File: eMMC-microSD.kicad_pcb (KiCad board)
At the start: 4 copper layers, 95 x 41.5 mm, 197 parts, among them J1 Micro_SD_Card, J2 Micro_SD_Card, J3 Micro_SD_Card, J4 Micro_SD_Card, J5 Micro_SD_Card, U1 eMMC_5.1_BGA153, U2 eMMC_5.1_BGA153, U3 eMMC_5.1_BGA153, U4 eMMC_5.1_BGA153, U5 eMMC_5.1_BGA153

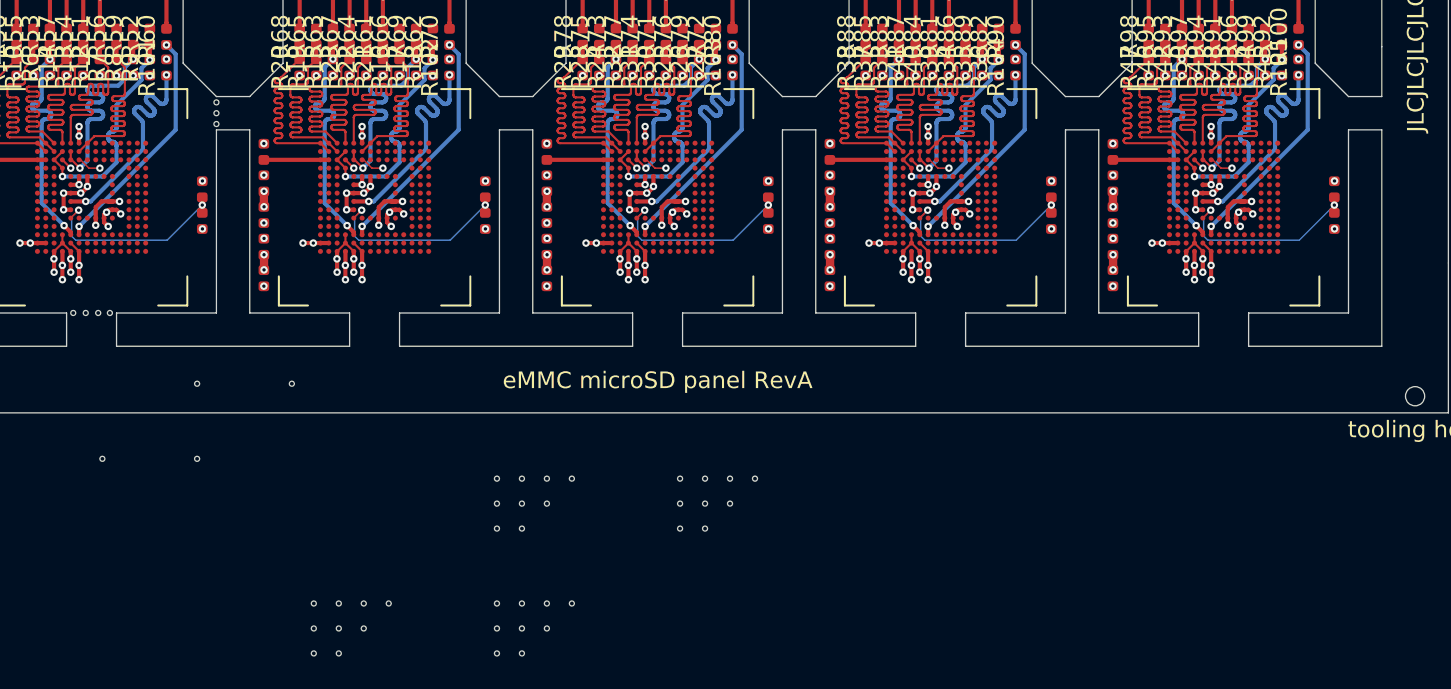
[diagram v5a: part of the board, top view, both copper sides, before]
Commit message: Plce remaining tooling holes
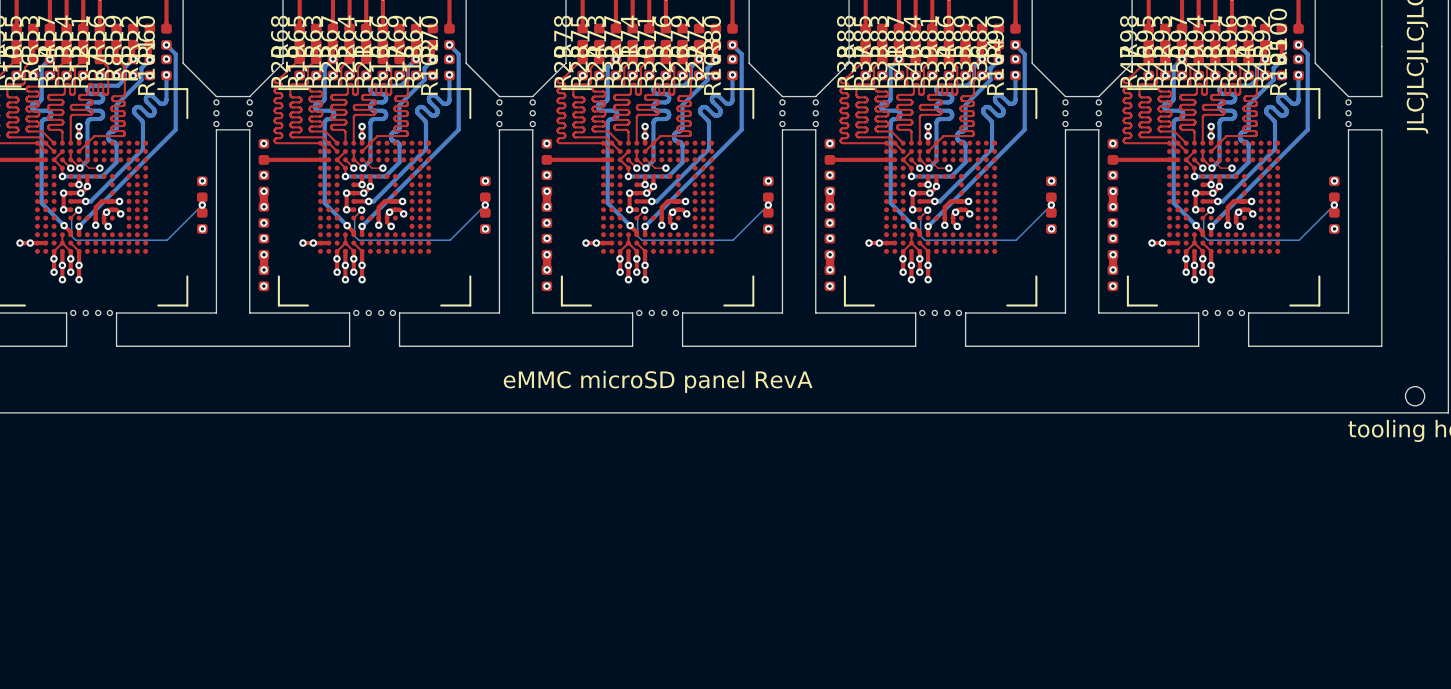
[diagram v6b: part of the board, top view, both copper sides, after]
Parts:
- moved H52 56.5 mm to (162.9, 148.0)
- moved H35 47.1 mm to (153.0, 136.0)
- moved H32 46.5 mm to (153.0, 135.3)
- moved H51 45.9 mm to (145.9, 148.0)
- moved H45 45.7 mm to (170.0, 136.7)
- moved H41 44.8 mm to (170.0, 135.3)
- moved H36 43.5 mm to (153.0, 136.7)
- moved H44 43.2 mm to (170.0, 136.0)
- moved H38 36.4 mm to (138.0, 136.0), turned to 90 degrees
- moved H34 36.2 mm to (138.0, 135.3), turned to 90 degrees
- moved H42 34.8 mm to (162.2, 148.0)
- moved H14 34.5 mm to (119.0, 135.3)
- moved H31 34.3 mm to (138.0, 136.7), turned to 90 degrees
- moved H40 33.9 mm to (155.0, 136.7), turned to 90 degrees
- moved H43 33.8 mm to (155.0, 135.3), turned to 90 degrees
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
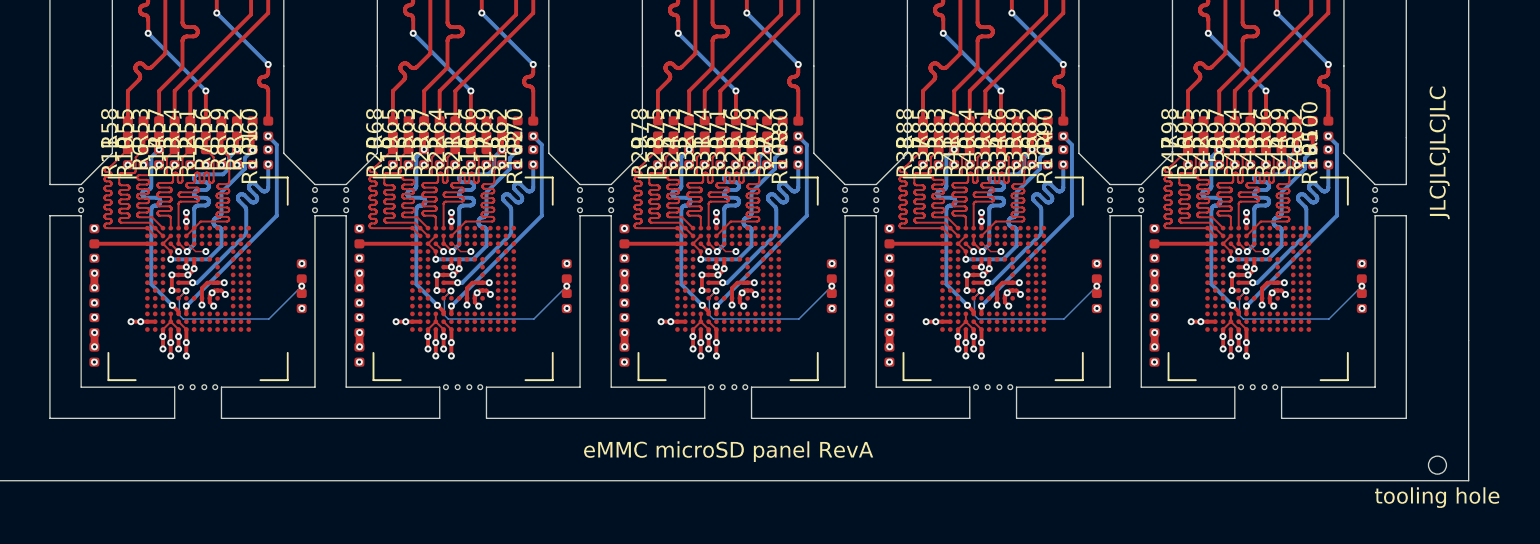
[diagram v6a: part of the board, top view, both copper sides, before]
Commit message: Hide all references
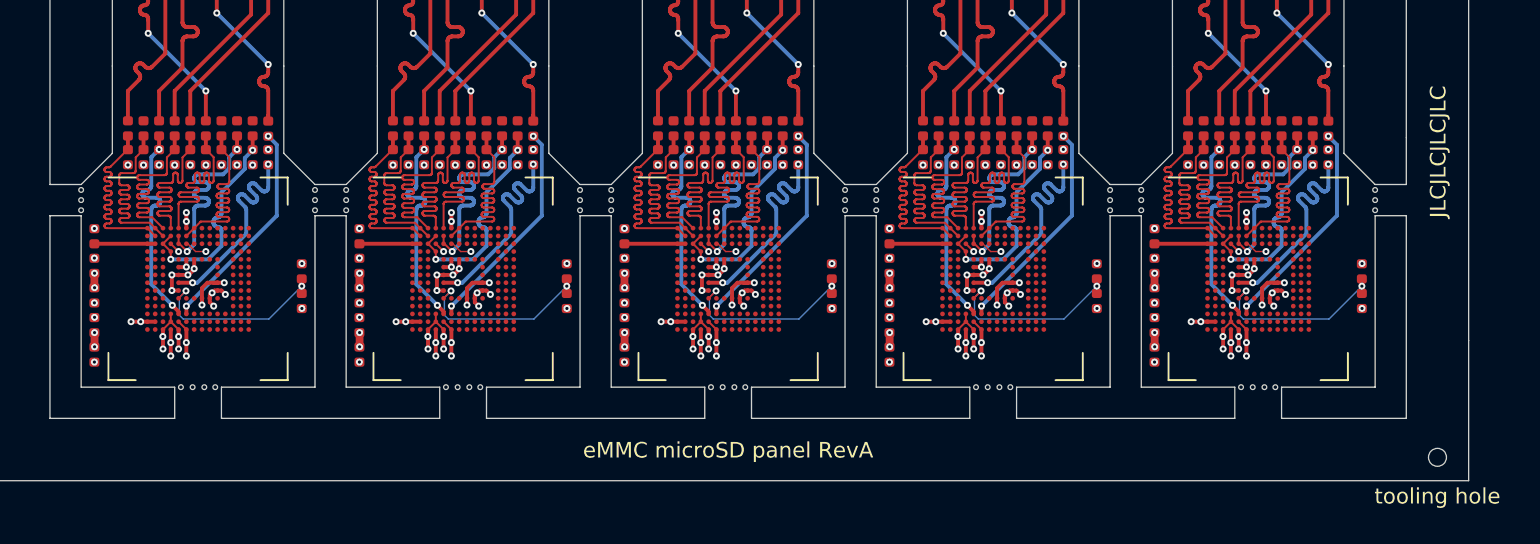
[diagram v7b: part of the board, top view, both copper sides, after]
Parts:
- moved H2 0.50 mm to (174.0, 152.5)

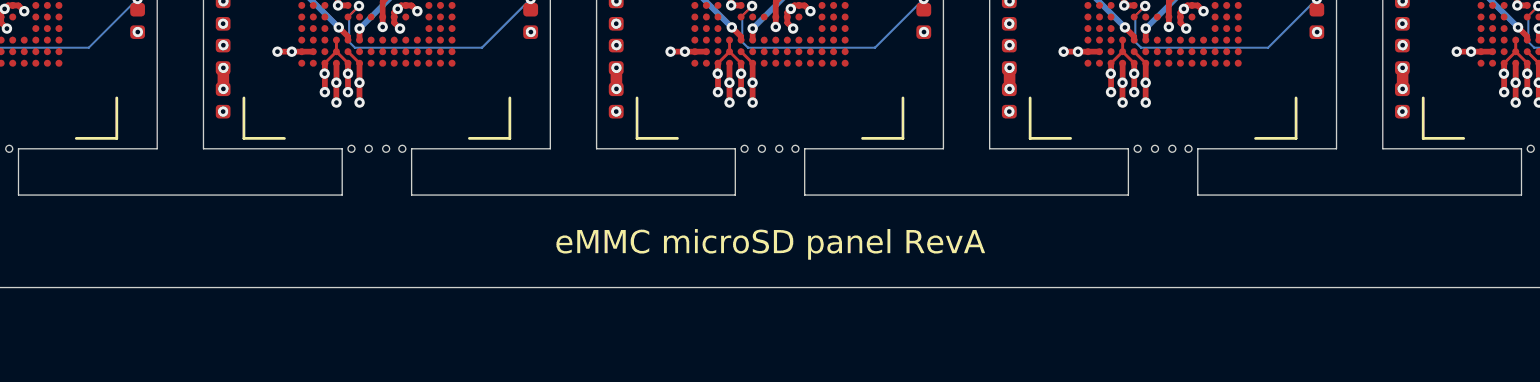
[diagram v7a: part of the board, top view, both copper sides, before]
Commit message: Fix silkscreen
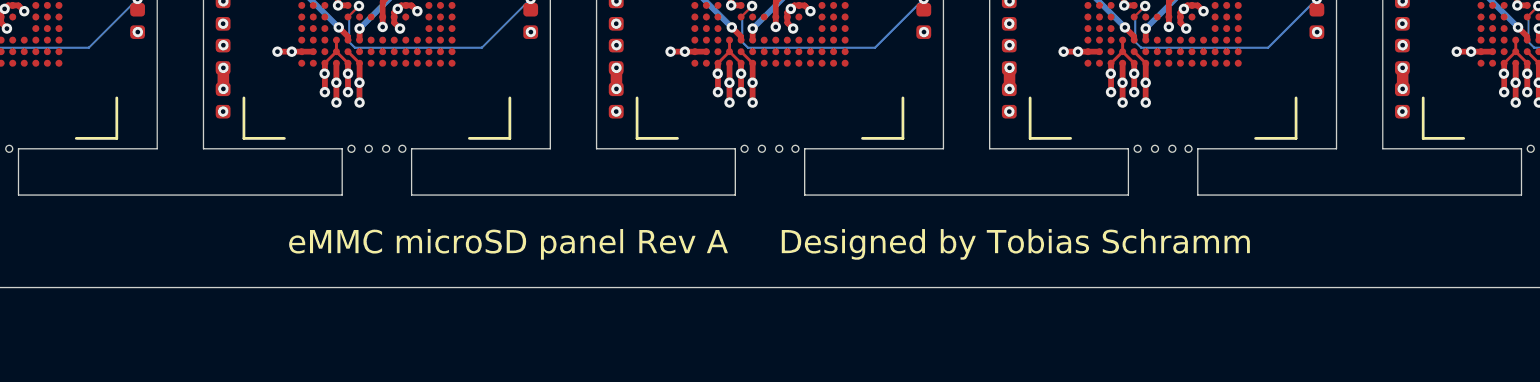
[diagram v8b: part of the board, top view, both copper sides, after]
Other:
- board text added: "eMMC microSD panel Rev A Designed by Tobias Schramm"
- board text removed: "eMMC microSD panel RevA"
